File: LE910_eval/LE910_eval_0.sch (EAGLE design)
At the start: 1 part, among them U1 LE910_V2

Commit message: 回路図修正
・SIMスロット、アンテナコネクターを追加、配線
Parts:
- added C1: 0.1uF, Parts:CAP_0603_DEV
- added C2, C3, C4: 33pF, Parts:CAP_0603_DEV
- added CN1: FMS008-6001-0, Connectors:FMS008-6001-0
- added CN2, CN3: U.FL-R-SMT-1, Connectors:U.FL-R-SMT-1
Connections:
- net 0V: now also C1.2, C2.2, C3.2, C4.2, CN1.C5, CN1.SW2, CN2.GND1, CN2.GND2, CN3.GND1, CN3.GND2
- net ANTENNA: now also CN2.ANT
- net ANT_DIV: now also CN3.ANT
- net SIMCLK: now also CN1.C3
- net SIMIN: now also CN1.SW1
- net SIMIO: now also CN1.C7
- net SIMRST: now also C2.1, C3.1, C4.1, CN1.C2
- net SIMVCC: now also C1.1, CN1.C1
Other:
- note added: "C4, C6, C8は接続しません"
- note added: "コネクター配線図"
- note removed: "外部I/Fコネクター配線図"
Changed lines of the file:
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@@
 <setting verticaltext="up"/>
 </settings>
-<grid distance="0.1" unitdist="inch" unit="inch" style="lines" multiple="1" display="no" altdistance="0.01" altunitdist="inch" altunit="inch"/>
+<grid distance="0.1" unitdist="inch" unit="inch" style="lines" multiple="1" display="yes" altdistance="0.01" altunitdist="inch" altunit="inch"/>
 <layers>
 <layer number="1" name="Top" color="4" fill="1" visible="no" active="no"/>
@@
 <part name="FRAME1" library="Generic" deviceset="A4L-LOC" device=""/>
 <part name="FRAME2" library="Generic" deviceset="A4L-LOC" device=""/>
+<part name="CN1" library="Connectors" deviceset="FMS008-6001-0" device=""/>
+<part name="GND1" library="Supply" deviceset="0V" device=""/>
+<part name="C1" library="Parts" deviceset="CAP" device="_0603_DEV" value="0.1uF"/>
+<part name="C2" library="Parts" deviceset="CAP" device="_0603_DEV" value="33pF"/>
+<part name="C3" library="Parts" deviceset="CAP" device="_0603_DEV" value="33pF"/>
+<part name="C4" library="Parts" deviceset="CAP" device="_0603_DEV" value="33pF"/>
+<part name="CN2" library="Connectors" deviceset="U.FL-R-SMT-1" device=""/>
+<part name="CN3" library="Connectors" deviceset="U.FL-R-SMT-1" device=""/>
+<part name="GND2" library="Supply" deviceset="0V" device=""/>
+<part name="GND3" library="Supply" deviceset="0V" device=""/>
 </parts>
 <sheets>
@@
 <sheet>
 <plain>
-<text x="167.64" y="12.7" size="2.54" layer="150">外部I/Fコネクター配線図</text>
+<text x="172.72" y="12.7" size="2.54" layer="150">コネクター配線図</text>
+<text x="91.44" y="121.92" size="1.778" layer="150" align="top-left">C4, C6, C8は接続しません</text>
 </plain>
 <instances>
 <instance part="FRAME2" gate="G$1" x="0" y="0"/>
+<instance part="CN1" gate="G$1" x="111.76" y="147.32"/>
+<instance part="GND1" gate="1" x="86.36" y="111.76"/>
+<instance part="C1" gate="G$1" x="45.72" y="137.16"/>
+<instance part="C2" gate="G$1" x="55.88" y="137.16"/>
+<instance part="C3" gate="G$1" x="66.04" y="137.16"/>
+<instance part="C4" gate="G$1" x="76.2" y="137.16"/>
+<instance part="CN2" gate="G$1" x="55.88" y="30.48"/>
+<instance part="CN3" gate="G$1" x="109.22" y="30.48"/>
+<instance part="GND2" gate="1" x="71.12" y="17.78"/>
+<instance part="GND3" gate="1" x="124.46" y="17.78"/>
 </instances>
 <busses>
 </busses>
 <nets>
+<net name="SIMIN" class="0">
+<segment>
+<pinref part="CN1" gate="G$1" pin="SW1"/>
+<wire x1="99.06" y1="134.62" x2="88.9" y2="134.62" width="0.1524" layer="91"/>
+<label x="88.9" y="134.62" size="1.778" layer="95"/>
+</segment>
+</net>
+<net name="0V" class="0">
+<segment>
+<pinref part="CN1" gate="G$1" pin="SW2"/>
+<pinref part="GND1" gate="1" pin="0V"/>
+<wire x1="99.06" y1="132.08" x2="86.36" y2="132.08" width="0.1524" layer="91"/>
+<wire x1="86.36" y1="132.08" x2="86.36" y2="121.92" width="0.1524" layer="91"/>
+<pinref part="CN1" gate="G$1" pin="C5"/>
+<wire x1="86.36" y1="121.92" x2="86.36" y2="114.3" width="0.1524" layer="91"/>
+<wire x1="99.06" y1="152.4" x2="86.36" y2="152.4" width="0.1524" layer="91"/>
+<wire x1="86.36" y1="152.4" x2="86.36" y2="132.08" width="0.1524" layer="91"/>
+<junction x="86.36" y="132.08"/>
+<pinref part="C1" gate="G$1" pin="2"/>
+<wire x1="45.72" y1="129.54" x2="45.72" y2="121.92" width="0.1524" layer="91"/>
+<wire x1="45.72" y1="121.92" x2="55.88" y2="121.92" width="0.1524" layer="91"/>
+<junction x="86.36" y="121.92"/>
+<pinref part="C2" gate="G$1" pin="2"/>
+<wire x1="55.88" y1="121.92" x2="66.04" y2="121.92" width="0.1524" layer="91"/>
+<wire x1="66.04" y1="121.92" x2="76.2" y2="121.92" width="0.1524" layer="91"/>
+<wire x1="76.2" y1="121.92" x2="86.36" y2="121.92" width="0.1524" layer="91"/>
+<wire x1="55.88" y1="129.54" x2="55.88" y2="121.92" width="0.1524" layer="91"/>
+<junction x="55.88" y="121.92"/>
+<pinref part="C3" gate="G$1" pin="2"/>
+<wire x1="66.04" y1="129.54" x2="66.04" y2="121.92" width="0.1524" layer="91"/>
+<junction x="66.04" y="121.92"/>
+<pinref part="C4" gate="G$1" pin="2"/>
+<wire x1="76.2" y1="129.54" x2="76.2" y2="121.92" width="0.1524" layer="91"/>
+<junction x="76.2" y="121.92"/>
+</segment>
+<segment>
+<pinref part="CN2" gate="G$1" pin="GND1"/>
+<pinref part="GND2" gate="1" pin="0V"/>
+<wire x1="63.5" y1="33.02" x2="71.12" y2="33.02" width="0.1524" layer="91"/>
+<wire x1="71.12" y1="33.02" x2="71.12" y2="27.94" width="0.1524" layer="91"/>
+<pinref part="CN2" gate="G$1" pin="GND2"/>
+<wire x1="71.12" y1="27.94" x2="71.12" y2="20.32" width="0.1524" layer="91"/>
+<wire x1="63.5" y1="27.94" x2="71.12" y2="27.94" width="0.1524" layer="91"/>
+<junction x="71.12" y="27.94"/>
+</segment>
+<segment>
+<pinref part="CN3" gate="G$1" pin="GND1"/>
+<pinref part="GND3" gate="1" pin="0V"/>
+<wire x1="116.84" y1="33.02" x2="124.46" y2="33.02" width="0.1524" layer="91"/>
+<wire x1="124.46" y1="33.02" x2="124.46" y2="27.94" width="0.1524" layer="91"/>
+<pinref part="CN3" gate="G$1" pin="GND2"/>
+<wire x1="124.46" y1="27.94" x2="124.46" y2="20.32" width="0.1524" layer="91"/>
+<wire x1="116.84" y1="27.94" x2="124.46" y2="27.94" width="0.1524" layer="91"/>
+<junction x="124.46" y="27.94"/>
+</segment>
+</net>
+<net name="SIMVCC" class="0">
+<segment>
+<pinref part="CN1" gate="G$1" pin="C1"/>
+<wire x1="99.06" y1="154.94" x2="45.72" y2="154.94" width="0.1524" layer="91"/>
+<label x="33.02" y="154.94" size="1.778" layer="95"/>
+<pinref part="C1" gate="G$1" pin="1"/>
+<wire x1="45.72" y1="154.94" x2="30.48" y2="154.94" width="0.1524" layer="91"/>
+<wire x1="45.72" y1="154.94" x2="45.72" y2="137.16" width="0.1524" layer="91"/>
+<junction x="45.72" y="154.94"/>
+</segment>
+</net>
+<net name="SIMRST" class="0">
+<segment>
+<pinref part="CN1" gate="G$1" pin="C2"/>
+<wire x1="99.06" y1="149.86" x2="76.2" y2="149.86" width="0.1524" layer="91"/>
+<label x="33.02" y="149.86" size="1.778" layer="95"/>
+<pinref part="C2" gate="G$1" pin="1"/>
+<wire x1="76.2" y1="149.86" x2="66.04" y2="149.86" width="0.1524" layer="91"/>
+<wire x1="66.04" y1="149.86" x2="55.88" y2="149.86" width="0.1524" layer="91"/>
+<wire x1="55.88" y1="149.86" x2="30.48" y2="149.86" width="0.1524" layer="91"/>
+<wire x1="55.88" y1="149.86" x2="55.88" y2="137.16" width="0.1524" layer="91"/>
+<junction x="55.88" y="149.86"/>
+<pinref part="C3" gate="G$1" pin="1"/>
+<wire x1="66.04" y1="149.86" x2="66.04" y2="137.16" width="0.1524" layer="91"/>
+<junction x="66.04" y="149.86"/>
+<pinref part="C4" gate="G$1" pin="1"/>
+<wire x1="76.2" y1="149.86" x2="76.2" y2="137.16" width="0.1524" layer="91"/>
+<junction x="76.2" y="149.86"/>
+</segment>
+</net>
+<net name="SIMCLK" class="0">
+<segment>
+<pinref part="CN1" gate="G$1" pin="C3"/>
+<wire x1="99.06" y1="144.78" x2="30.48" y2="144.78" width="0.1524" layer="91"/>
+<label x="33.02" y="144.78" size="1.778" layer="95"/>
+</segment>
+</net>
+<net name="SIMIO" class="0">
+<segment>
+<pinref part="CN1" gate="G$1" pin="C7"/>
+<wire x1="99.06" y1="142.24" x2="30.48" y2="142.24" width="0.1524" layer="91"/>
+<label x="33.02" y="142.24" size="1.778" layer="95"/>
+</segment>
+</net>
+<net name="ANTENNA" class="0">
+<segment>
+<pinref part="CN2" gate="G$1" pin="ANT"/>
+<wire x1="48.26" y1="30.48" x2="30.48" y2="30.48" width="0.1524" layer="91"/>
+<label x="33.02" y="30.48" size="1.778" layer="95"/>
+</segment>
+</net>
+<net name="ANT_DIV" class="0">
+<segment>
+<pinref part="CN3" gate="G$1" pin="ANT"/>
+<wire x1="101.6" y1="30.48" x2="83.82" y2="30.48" width="0.1524" layer="91"/>
+<label x="86.36" y="30.48" size="1.778" layer="95"/>
+</segment>
+</net>
 </nets>
 </sheet>

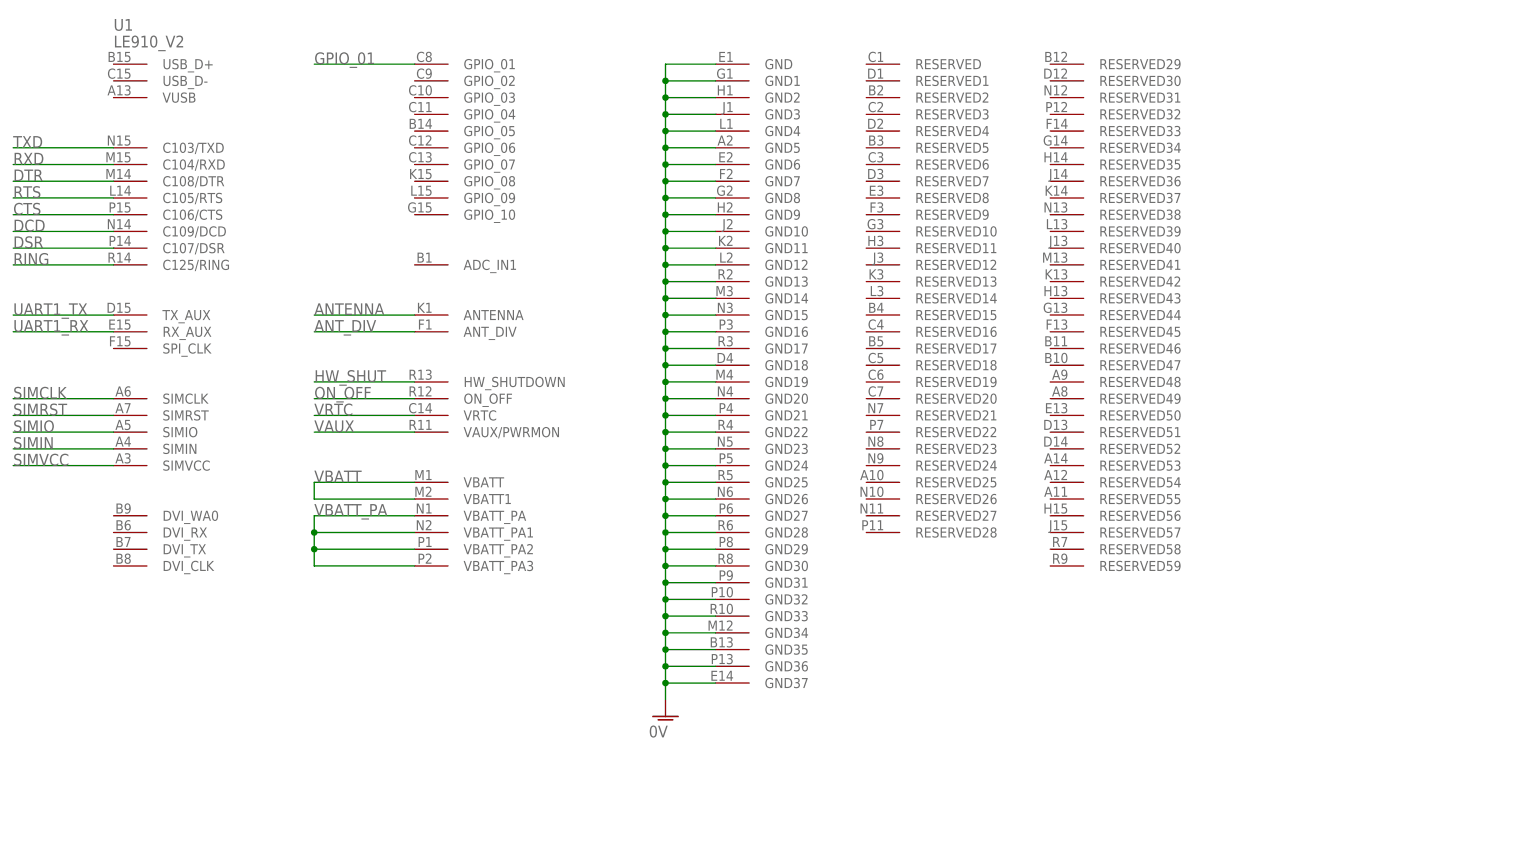
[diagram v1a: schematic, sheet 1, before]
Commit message: 回路図修正
・動作確認用LED、スイッチ類を追加
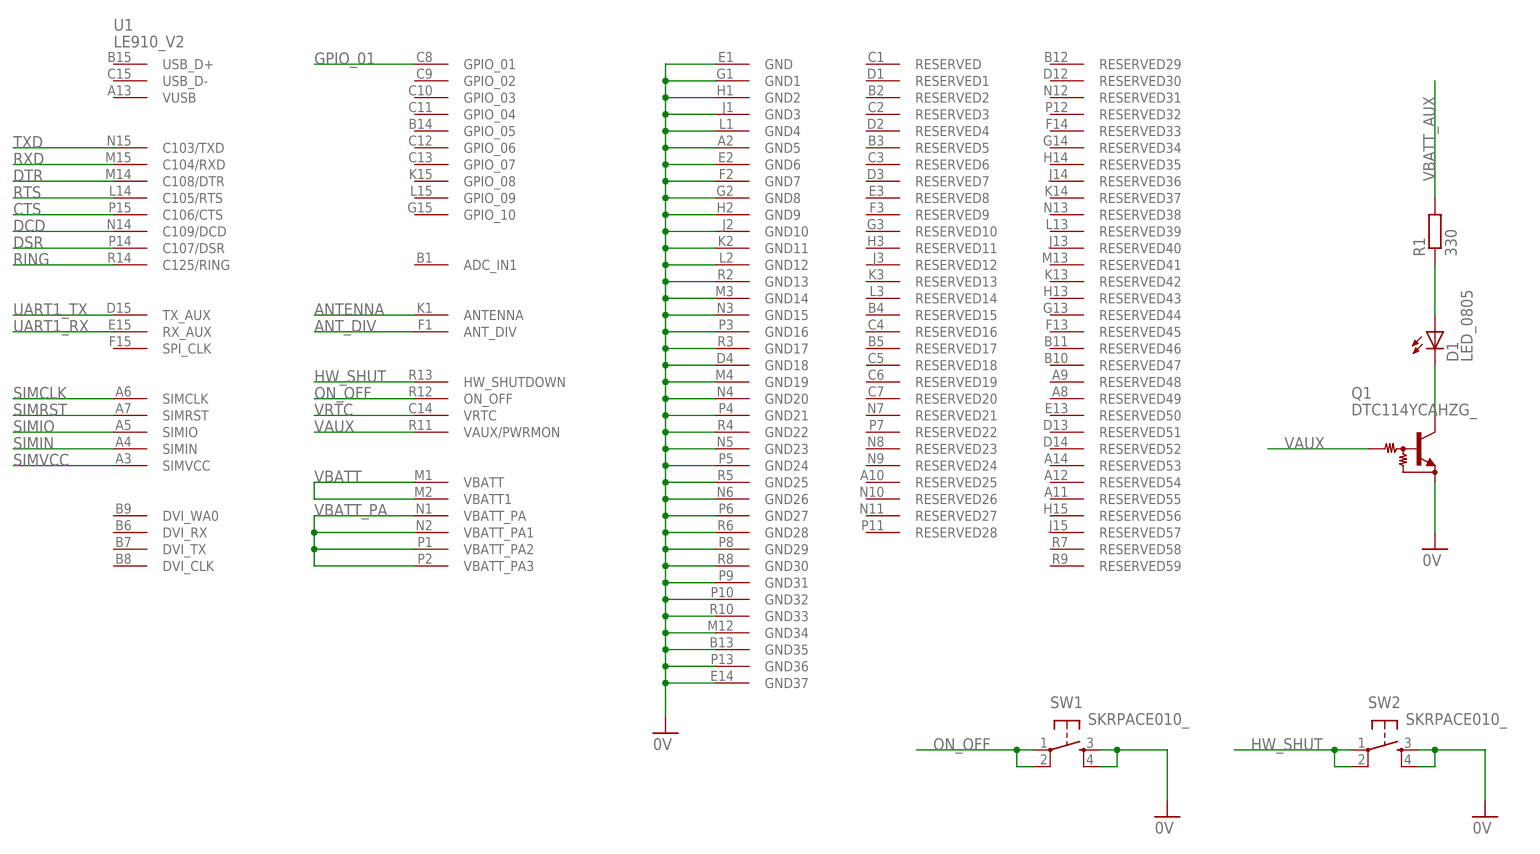
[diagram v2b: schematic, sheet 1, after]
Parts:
- added D1: LED_0805, Parts:LED_0805
- added Q1: DTC114YCAHZG_, Parts:DTC114YCAHZG_
- added R1: 330, Parts:RESISTOR_0603_DEV
- added SW1, SW2: SKRPACE010_, Parts:SKRPACE010_
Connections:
- new net N$1: D1.A, R1.1
- new net N$2: D1.C, Q1.C
- new net VBATT_AUX: R1.2
- net 0V: now also Q1.E, SW1.S, SW1.S1, SW2.S, SW2.S1
- net HW_SHUT: now also SW2.P, SW2.P1
- net ON_OFF: now also SW1.P, SW1.P1
- net VAUX: now also Q1.B
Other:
- note added: "強制停止スイッチ LOWを200ms以上 保持するとシャットダウン"
- note added: "起動スイッチ LOWを5秒以上 保持するとパワーオン"
- note added: "起動状態LED PWRMONがHIGHで LEDが点灯"

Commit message: 回路図修正
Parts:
- removed CN1: FMS008-6001-0, Connectors:FMS008-6001-0
- removed CN2, CN3: U.FL-R-SMT-1, Connectors:U.FL-R-SMT-1
- added C10, C14: 2.2uF, Parts:CAP_0603_DEV
- added C11: 100uF, Parts:TPSW107K006R0150
- added C12, C13, C16, C19, C6, C7, C8, C9: 33pF, Parts:CAP_0603_DEV
- added C15, C17, C18, C20: 1uF, Parts:CAP_0603_DEV
- added C5: 0.1uF, Parts:CAP_0603_DEV
- added CN4: FMS008-6001-0, Connectors:FMS008-6001-0
- added CN5, CN6: U.FL-R-SMT-1, Connectors:U.FL-R-SMT-1
- added D2: STPS140A_, Parts:STPS140A_
- added F1: SF-1206F200-2_, Parts:SF-1206F200-2_
- added L1, L2: BLM18EG101TN1D_, Parts:BLM18EG101TN1D_
- added R10, R4, R5, R6, R7, R8, R9: 0, Parts:RESISTOR_0603_DEV
- added R2: 16k, Parts:RESISTOR_0603_DEV
- added R3: 4.3k, Parts:RESISTOR_0603_DEV
- added U2: LDL112PVR_, Parts:LDL112PVR_
- added U3: MIC5366-1.8YC5_, Parts:MIC5366-1.8YC5_
- added U4: MIC5366-3.3YC5, Parts:MIC5366-3.3YC5
- C1: value 0.1uF -> 1uF
- C2: value 33pF -> 1uF
- C3: value 33pF -> 100uF; device Parts:CAP_0603_DEV -> Parts:TPSW107K006R0150
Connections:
- new net +1V8: C17.1, U3.VOUT
- new net +3V3: C18.1, U4.VOUT
- new net +3V8: C2.1, R2.2, R4.1, R5.1, R6.1, U2.VOUT
- new net +5V: F1.1
- new net N$3: C1.1, D2.C, F1.2, U2.EN, U2.VIN
- new net N$4: R7.2, R8.2, U3.EN
- new net N$7: R2.1, R3.2, U2.ADJ
- new net N$8: R10.2, R9.2, U4.EN
- new net REF_SRC_3V8: C15.1, C16.1, C19.1, C20.1, R6.2, R8.1, R9.1, U3.VIN, U4.VIN
- new net VBATT_3V8: C3.+, C4.1, L1.1, R4.2
- new net VBATT_PA_3V8: C11.+, C12.1, L2.1, R5.2
- net 0V: now also C10.2, C11.-, C12.2, C13.2, C14.2, C15.2, C16.2, C17.2, C18.2, C19.2, C20.2, C3.-, C5.2, C6.2, C7.2, C8.2, C9.2, CN4.C5, CN4.SW2, CN5.GND1, CN5.GND2, CN6.GND1, CN6.GND2, D2.A, R3.1, U2.GND, U2.GND0, U3.GND, U4.GND; no longer C3.2, CN1.C5, CN1.SW2, CN2.GND1, CN2.GND2, CN3.GND1, CN3.GND2
- net ANTENNA: now also CN5.ANT; no longer CN2.ANT
- net ANT_DIV: now also CN6.ANT; no longer CN3.ANT
- net SIMCLK: now also CN4.C3; no longer CN1.C3
- net SIMIN: now also CN4.SW1; no longer CN1.SW1
- net SIMIO: now also CN4.C7; no longer CN1.C7
- net SIMRST: now also C6.1, C7.1, C8.1, CN4.C2; no longer C2.1, C3.1, C4.1, CN1.C2
- net SIMVCC: now also C5.1, CN4.C1; no longer C1.1, CN1.C1
- net VAUX: now also R10.1, R7.1
- net VBATT: now also C10.1, C9.1, L1.2
- net VBATT_PA: now also C13.1, C14.1, L2.2
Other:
- note added: "EN=Highで 1.8Vが出力される"
- note added: "EN=Highで 3.3Vが出力される"
- note added: "ノイズフィルター回路"
- note added: "パスコンは 以下を選定 1uF=X5R 33pF=COG 50V"
- note added: "パスコンは以下を選定 0.1uF=X7R 33pF=COG 50V"
- note added: "パスコンは以下を選定 2.2uF=X5R 33pF=COG 50V"
- note added: "基準電圧用降圧回路（1.8V）"
- note added: "基準電圧用降圧回路（3.3V）"
- note added: "降圧回路（最大5V--->3.8V）"
- note added: "電源系統配線図"

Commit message: 回路図修正
・UART用のレベル変換回路を追加
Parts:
- removed SW1, SW2: SKRPACE010_, Parts:SKRPACE010_
- added C21, C23, C25, C26, C27, C28: 0.1uF, Parts:CAP_0603_DEV
- added C22, C24: (no value), Parts:CAP_0603_DEV
- added CN1: UART0_IF, PartsForProto:RS_232C_IF
- added CN2: UART1_IF, PartsForProto:UART_IF
- added D3: LED_0805, Parts:LED_0805
- added Q2: DTC114YCAHZG_, Parts:DTC114YCAHZG_
- added R11: 330, Parts:RESISTOR_0603_DEV
- added R12, R13: 10k, Parts:RESISTOR_0603_DEV
- added SW3, SW4: SKRPACE010_, Parts:SKRPACE010_
- added U5, U6: SN74AVC4T245PW_, Parts:SN74AVC4T245PW_
- added U7, U8: SN74AVC1T45DCK_, Parts:SN74AVC1T45DCK_
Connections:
- net UART1_TX renamed TX_AUX
- removed net CTS: U1.C106/CTS
- removed net DCD: U1.C109/DCD
- removed net DSR: U1.C107/DSR
- removed net DTR: U1.C108/DTR
- removed net RTS: U1.C105/RTS
- removed net RXD: U1.C104/RXD
- removed net TXD: U1.C103/TXD
- removed net UART1_RX: U1.RX_AUX
- removed net VBATT_AUX: R1.2
- new net C103/TXD: U1.C103/TXD, U6.2A1
- new net C104/RXD: U1.C104/RXD, U5.2A2
- new net C105/RTS: U1.C105/RTS, U6.1A2
- new net C106/CTS: U1.C106/CTS, U5.1A1
- new net C107/DSR: U1.C107/DSR, U5.2A1
- new net C108/DTR: U1.C108/DTR, U6.1A1
- new net C109/DCD: U1.C109/DCD, U5.1A2
- new net N$10: R12.2, U5.1!OE!, U5.2!OE!
- new net N$11: U5.1B1
- new net N$12: U5.1B2
- new net N$13: U5.2B1
- new net N$14: U5.2B2
- new net N$15: U6.1B1
- new net N$16: U6.1B2
- new net N$17: U6.2B1
- new net N$18: U8.B
- new net N$19: CN1.DCD
- new net N$2: D3.C, Q2.C
- new net N$20: CN1.RXD
- new net N$21: U7.B
- new net N$22: C21.1, U5.1DIR, U5.2DIR, U5.VCCA
- new net N$23: CN1.CTS
- new net N$24: CN1.RTS
- new net N$25: CN1.DSR
- new net N$26: CN1.GND
- new net N$27: CN1.DTR
- new net N$28: CN1.TXD
- new net N$29: CN2.GND
- new net N$30: CN2.RX
- new net N$31: CN2.TX
- new net N$6: D3.A, R11.1
- new net N$9: R13.2, U6.1!OE!, U6.2!OE!
- new net RX_AUX: U1.RX_AUX, U7.A, U8.A
- net +1V8: now also C23.1, C25.1, C27.1, U6.VCCA, U7.VCCA, U8.DIR, U8.VCCA
- net +3V3: now also C22.1, C24.1, C26.1, C28.1, U5.VCCB, U6.VCCB, U7.VCCB, U8.VCCB
- net +3V8: now also R1.2, R11.2
- net 0V: now also C21.2, C22.2, C23.2, C24.2, C25.2, C26.2, C27.2, C28.2, Q2.E, R12.1, R13.1, SW3.S, SW3.S1, SW4.S, SW4.S1, U5.GND, U5.GND1, U6.1DIR, U6.2DIR, U6.GND, U6.GND1, U7.DIR, U7.GND, U8.GND; no longer SW1.S, SW1.S1, SW2.S, SW2.S1
- net GPIO_01: now also Q1.B
- net HW_SHUT: now also SW4.P, SW4.P1; no longer SW2.P, SW2.P1
- net ON_OFF: now also SW3.P, SW3.P1; no longer SW1.P, SW1.P1
- net VAUX: now also Q2.B; no longer Q1.B
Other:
- note added: "SIMカードスロット回路"
- note added: "その他配線図"
- note added: "アンテナコネクター （U.FL規格を使用）"
- note added: "入力信号用（<---）レベル変換回路"
- note added: "出力信号用（--->）レベル変換回路"
- note added: "動作状態LED GPIO_0がHIGHでLEDが点灯 事前に AT#GPIO=1,0,2 を 実行する必要あり"
- note added: "起動状態LED VAUXがHIGHで LEDが点灯"
- note removed: "起動状態LED PWRMONがHIGHで LEDが点灯"
